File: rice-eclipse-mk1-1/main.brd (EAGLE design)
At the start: 170.1 x 119.4 mm, 210 parts, among them IC1 LMV321LICTRT, IC10 MCP6N11R, IC11 MCP6N11R, IC12 MCP6N11R, IC13 LMV321LICTRT, IC14 LMV321LICTRT, IC15 LMV321LICTRT, IC16 LMV321LICTRT, IC17 LMV321LICTRT, IC2 LMV321LICTRT, IC3 LMV321LICTRT, IC4 LMV321LICTRT, IC5 MCP6N11R, IC6 LMV321LICTRT, IC7 LMV321LICTRT, IC8 LMV321LICTRT, IC9 LMV321LICTRT, U2 1101M2S3CQE2, U6 1101M2S3CQE2

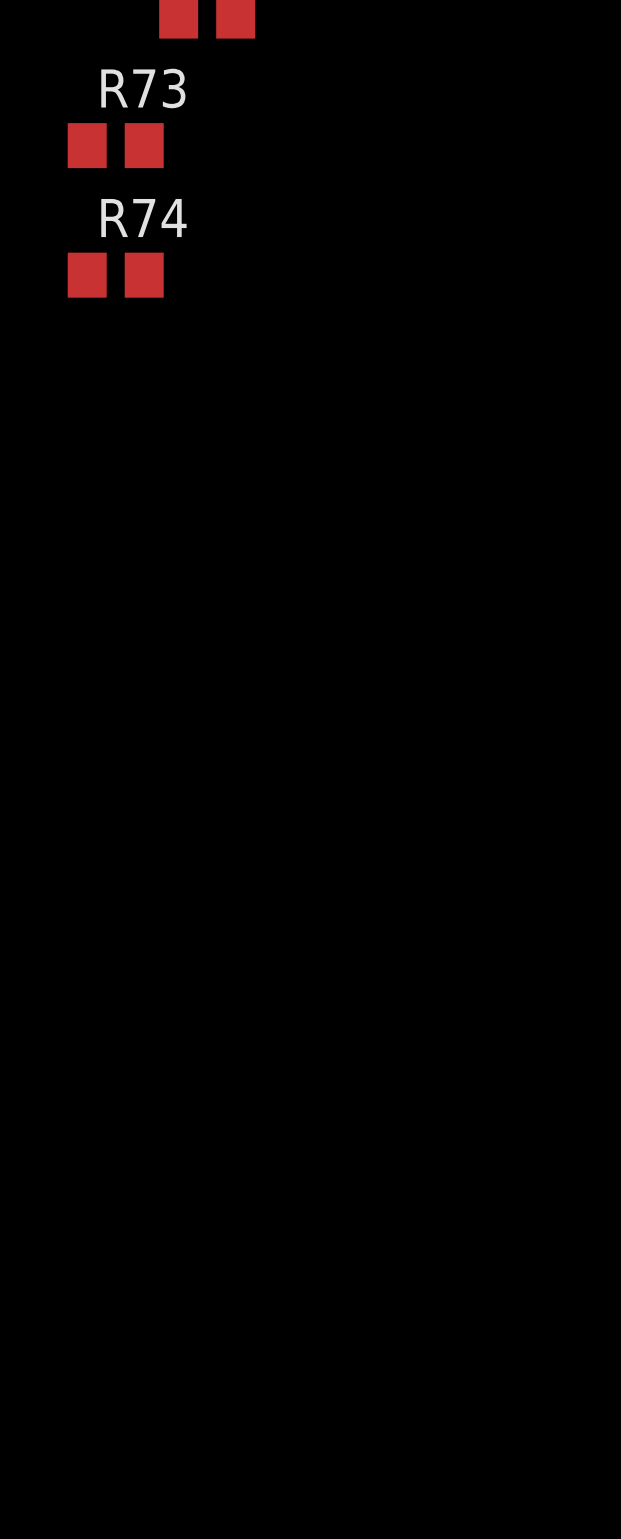
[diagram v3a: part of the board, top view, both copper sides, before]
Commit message: Add current and voltage sense circuitry
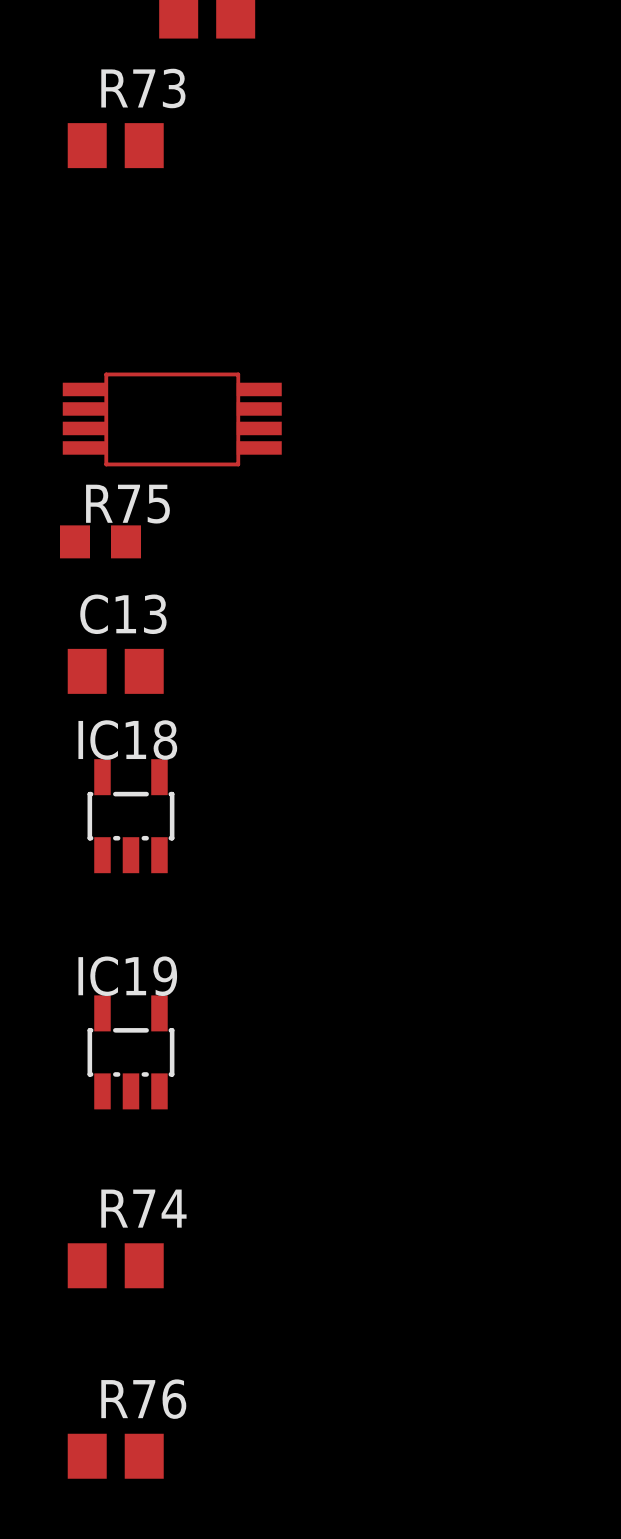
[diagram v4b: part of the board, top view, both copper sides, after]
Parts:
- added C13: (no value), rcl:C0805
- added IC18, IC19: LMV321LICTRT, st-microelectronics-extra:SOT23-5
- added R75: (no value), rcl:R0603
- added R76: 25k, rcl:R0805
- added U$10: INA240A1, INA240A1:INA240A1
- R74: value 0.005 -> 100k
- moved R74 33.0 mm to (-24.1, -175.0)
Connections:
- new net N$68: IC19.1, R74.2, R76.1
- new net N$69: IC19.4, R76.2
- net +3V3: now also C13.1, IC19.5, U$10.REF2, U$10.VS
- net ADC3_A6: now also U$10.OUT
- net GND: now also C13.2, IC19.2, IC19.3, U$10.GND, U$10.REF1
- net N$67: now also R75.1, U$10.IN-; no longer R74.1
- net SOLENOID_3_NEGATIVE: now also R74.1, R75.2, U$10.IN+; no longer R74.2
